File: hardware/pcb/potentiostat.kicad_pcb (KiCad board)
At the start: 2 copper layers, 94 parts, among them K1 CONN_3, P1 CONN_2, P10 CONN_2, P11 CONN_2, P12 CONN_2, P13 CONN_5X2, P14 CONN_5X2, P15 CONN_2X2, P16 CONN_2X2, P17 CONN_2, P18 CONN_2, P19 CONN_2, P2 CONN_2, P20 CONN_2, P21 CONN_2, P3 CONN_2, P4 CONN_2, P5 CONN_2, P6 CONN_2, P7 CONN_2, P8 CONN_2, P9 CONN_2, U1 ZXRE060, U10 OPA227, U11 OP07, U12 LT1995, U13 ADG44X, U2 TEENSY3.1, U3 MAX6176AASA+, U4 LT1995, U5 AD8250, U6 MEA1D05XXSC, U7 OPA129, U8 OPA129, U9 ADG44X

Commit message: Worked on pcb layout.
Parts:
- added 4-40: VAL**, 4-40, F.Cu at (174.0, 135.9)
- added 4-40: VAL**, 4-40, F.Cu at (54.6, 135.9)
- added 4-40: VAL**, 4-40, F.Cu at (54.6, 54.6)
- added 4-40: VAL**, 4-40, F.Cu at (174.0, 54.6)
- moved P1 565.5 mm to (189.2, 71.1), turned to 270 degrees
- moved P2 552.6 mm to (189.2, 82.5), turned to 270 degrees
- moved P3 539.7 mm to (189.2, 94.0), turned to 270 degrees
- moved K1 505.2 mm to (175.5, 117.6), turned to 270 degrees
- moved P8 481.5 mm to (139.7, 135.9), turned to 270 degrees
- moved P10 481.1 mm to (130.8, 54.6), turned to 90 degrees
- moved P9 472.7 mm to (139.7, 54.6), turned to 270 degrees
- moved C8 468.1 mm to (125.7, 62.2)
- moved C6 461.4 mm to (121.9, 62.2)
- moved C4 459.9 mm to (117.5, 74.3), turned to 0 degrees
- moved C2 457.2 mm to (117.5, 71.1), turned to 0 degrees
- moved U5 453.5 mm to (115.6, 66.0), turned to 270 degrees
- moved P7 452.1 mm to (113.0, 54.6), turned to 270 degrees
- moved P6 442.5 mm to (104.1, 54.6), turned to 270 degrees
- moved C5 433.4 mm to (102.2, 71.1), turned to 0 degrees
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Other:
- board outline added: 144.8 x 88.9 mm

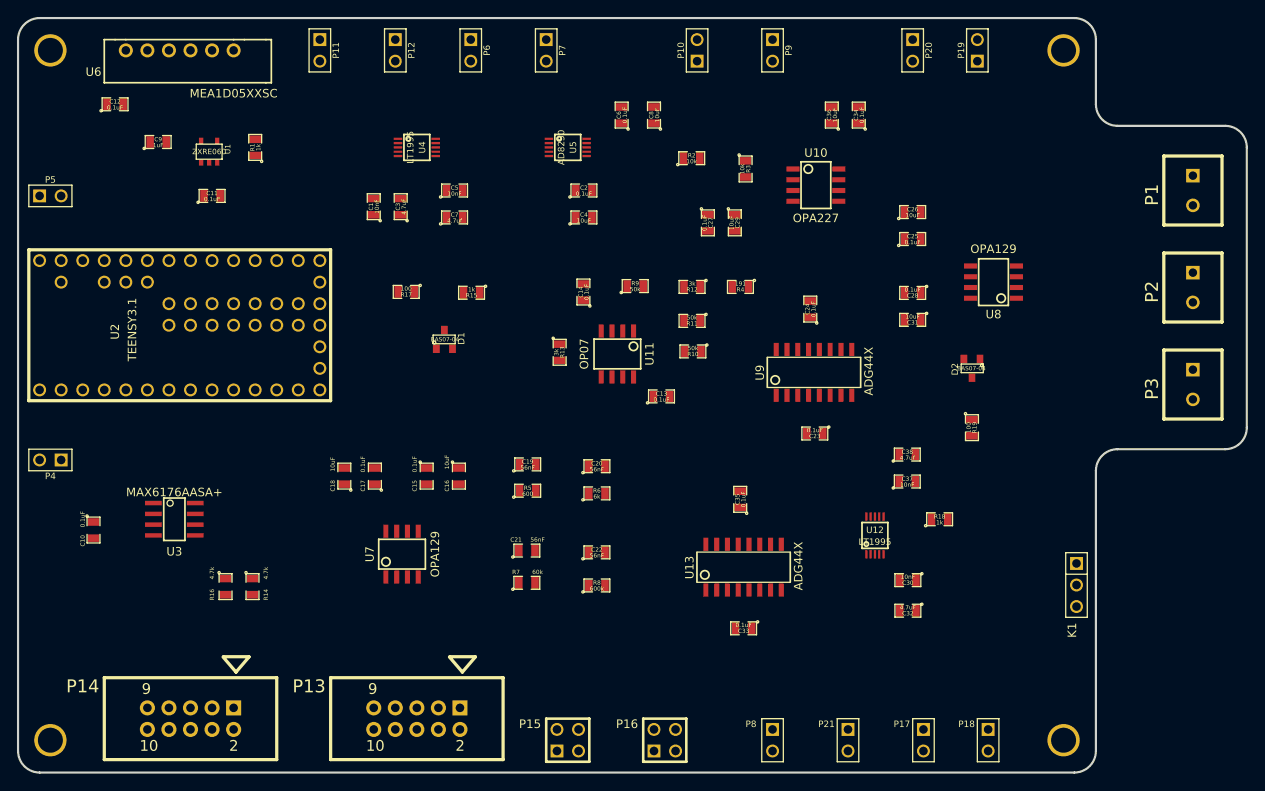
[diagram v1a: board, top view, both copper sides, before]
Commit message: Finished intial routing of pcb.
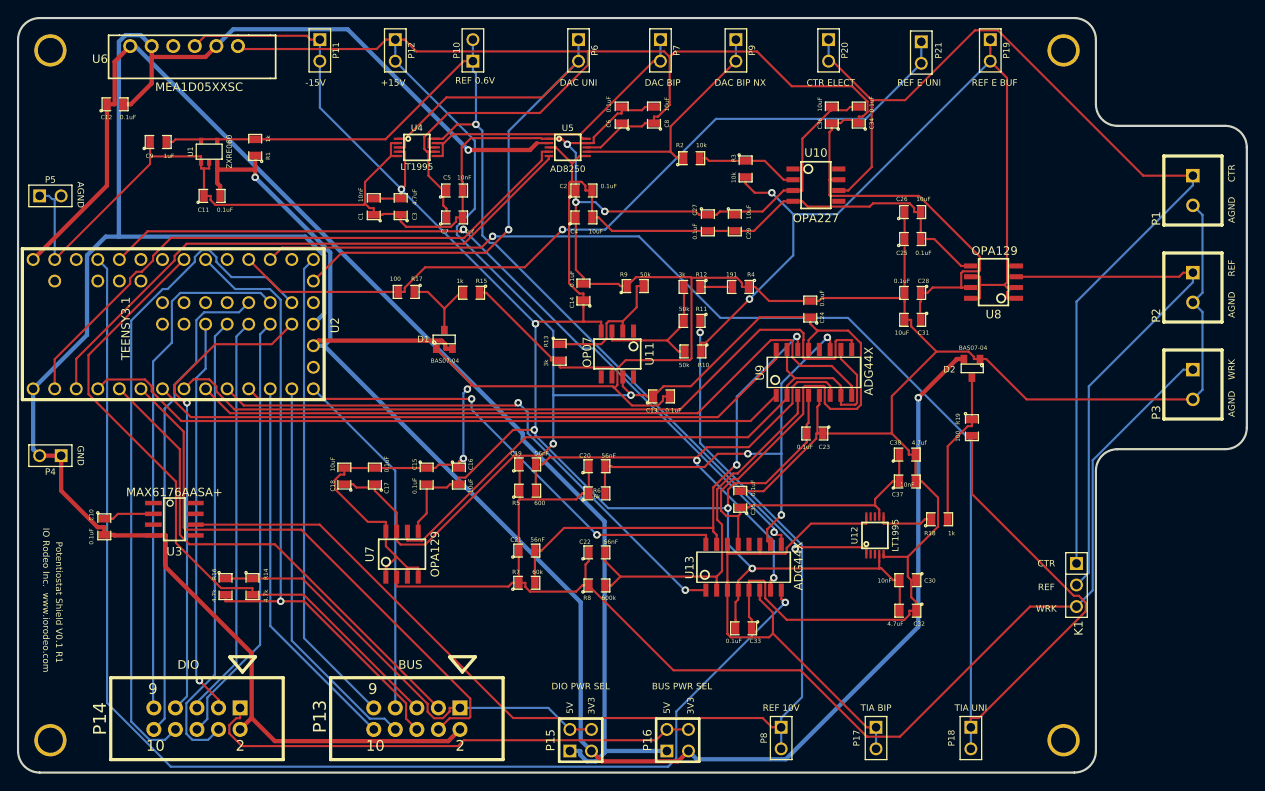
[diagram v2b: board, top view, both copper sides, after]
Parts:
- moved P21 81.5 mm to (157.2, 54.9)
- moved P10 26.4 mm to (104.4, 54.6)
- moved P7 13.5 mm to (126.5, 54.6)
- moved P6 12.7 mm to (116.8, 54.6)
- moved P20 9.91 mm to (146.3, 54.6)
- moved P17 5.59 mm to (151.9, 135.6)
- moved P9 4.32 mm to (135.4, 54.6)
- moved P18 2.05 mm to (163.1, 135.6)
- moved P15 1.52 mm to (117.1, 135.9)
- moved P16 1.52 mm to (128.5, 135.9)
- moved P19 1.52 mm to (165.4, 54.6), turned to 270 degrees
- moved C10 1.33 mm to (61.0, 110.7)
- moved P8 1.05 mm to (140.7, 135.6)
- moved U2 0.77 mm to (69.1, 86.9)
- moved P14 0.76 mm to (71.9, 133.3)
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- renumbered 4-40 to H1, 4-40 to H2, 4-40 to H3, 4-40 to H4
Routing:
- net /AGND: track 0.00 -> 493.9 mm, vias 0 -> 5
- net /+15V: track 0.00 -> 391.7 mm, vias 0 -> 2
- net /-15V: track 0.00 -> 282.5 mm, vias 0 -> 5
- net /GND: track 0.00 -> 231.4 mm, vias 0 -> 1
- net /3V3: track 0.00 -> 195.0 mm, vias 0 -> 2
- net /TIA_OUT_UNI: track 0.00 -> 176.4 mm, vias 0 -> 1
- net /WRK_ELECT: track 0.00 -> 160.1 mm
- net /5V: track 0.00 -> 149.8 mm
- net /TIA_SW2_IN4: track 0.00 -> 148.7 mm, vias 0 -> 1
- net /REF_10V: track 0.00 -> 135.3 mm, vias 0 -> 1
- net /REF_0V6: track 0.00 -> 133.9 mm, vias 0 -> 2
- net /CTR_ELECT: track 0.00 -> 122.1 mm
- net /REF_ELECT_BUF: track 0.00 -> 102.3 mm, vias 0 -> 2
- net /TIA_SW2_IN3: track 0.00 -> 95.8 mm, vias 0 -> 2
- net /REF_ELECT_UNI: track 0.00 -> 94.8 mm, vias 0 -> 1
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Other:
- net class Default: clearance 0.254 -> 0.2032
- net class Power added: clearance 0.2032, trace_width 0.508, via_dia 0.889, via_drill 0.635
- rule trace_clearance: 0.254 -> 0.2032
- board text added: "+15V"
- board text added: "-15V"
- board text added: "3V3"
- board text added: "5V"
- board text added: "AGND"
- board text added: "BUS"
- board text added: "BUS PWR SEL"
- board text added: "CTR"
- board text added: "CTR ELECT"
- board text added: "DAC BIP"
- board text added: "DAC BIP NX"
- board text added: "DAC UNI"
- board text added: "DIO"
- board text added: "DIO PWR SEL"
- board text added: "GND"
- board text added: "IO Rodeo Inc. www.iorodeo.com"
- board text added: "Potentiostat Shield V0.1 R1"
- board text added: "REF"
- board text added: "REF 0.6V"
- board text added: "REF 10V"
- board text added: "REF E BUF"
- board text added: "REF E UNI"
- board text added: "TIA BIP"
- board text added: "TIA UNI"
- board text added: "WRK"
